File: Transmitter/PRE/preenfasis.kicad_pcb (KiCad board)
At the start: 2 copper layers, 25 x 40 mm, 24 parts, among them J1 SMA H, J2 SMA H, J3 SMA H, J4 SMA H

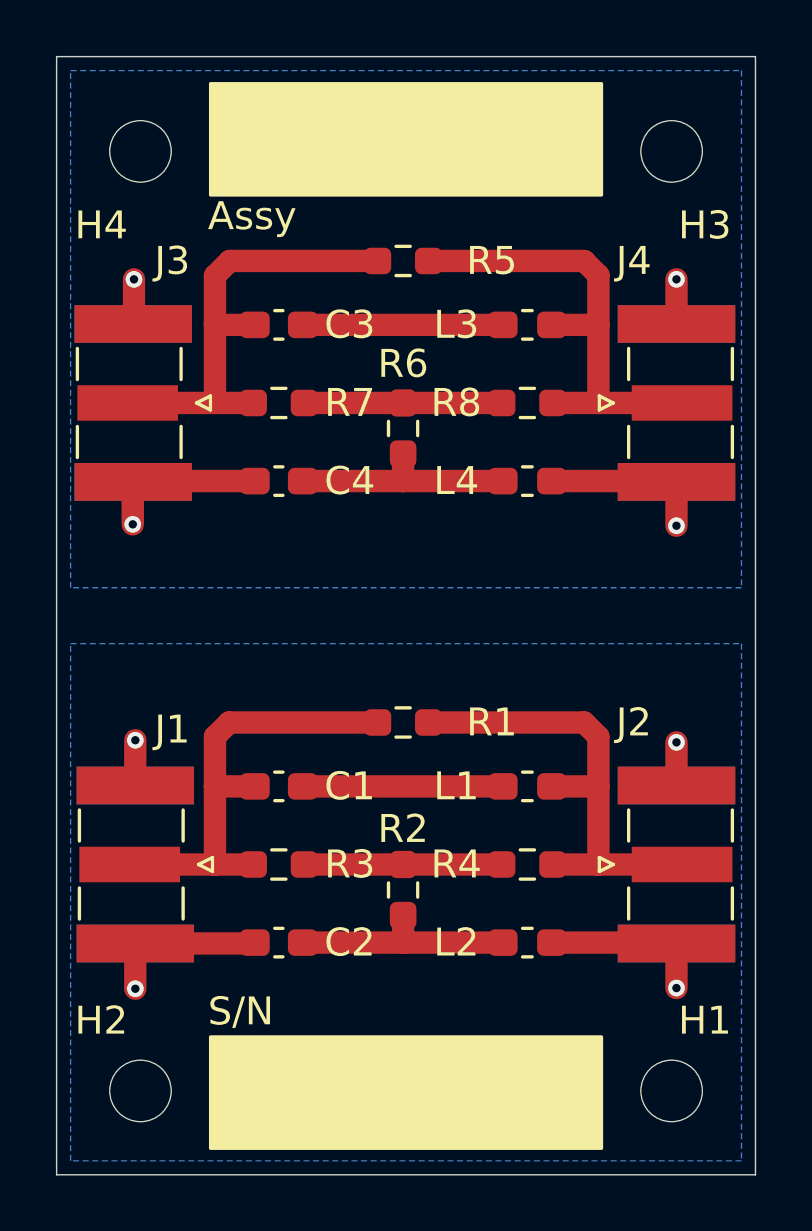
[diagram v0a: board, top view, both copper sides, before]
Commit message: v1.2 preenfasis
Se cambia el tamaño de los tornillos de M2 a M3
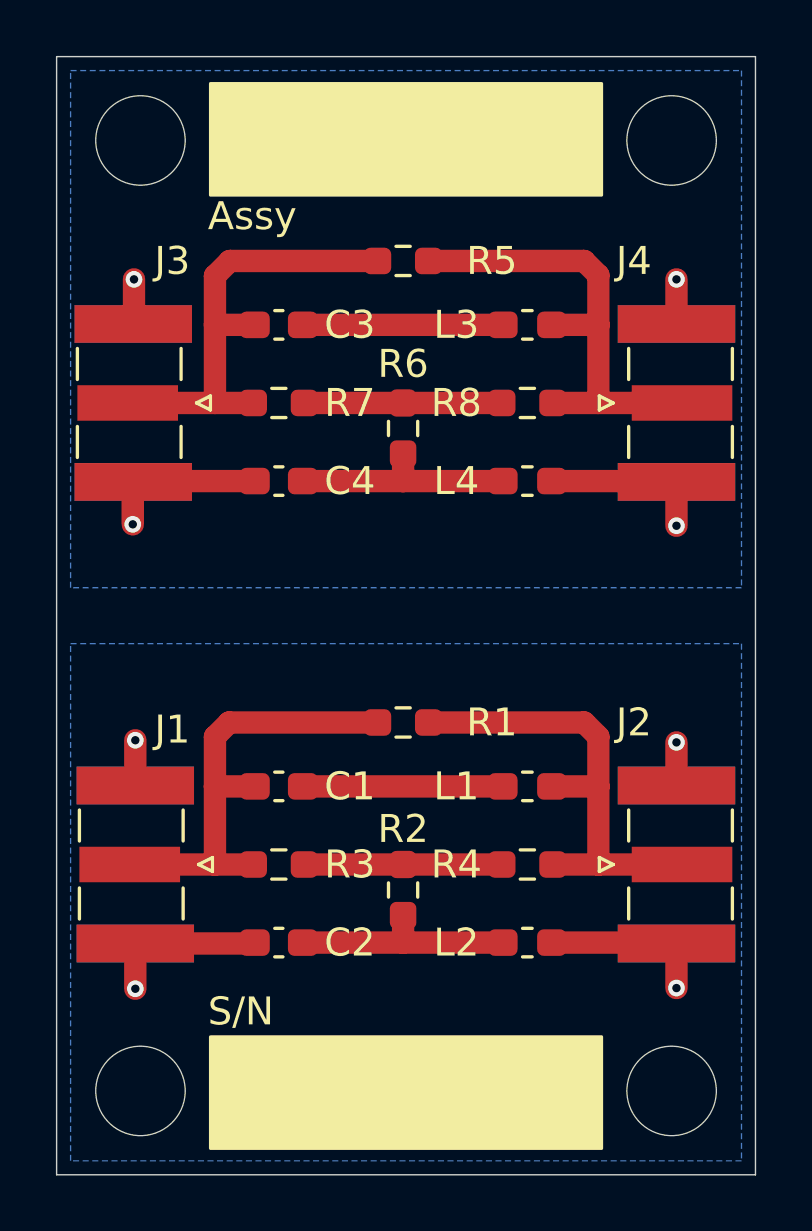
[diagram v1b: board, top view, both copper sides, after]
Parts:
- H1, H2, H3, H4: value M2 -> M3; footprint MountingHole:MountingHole_2.2mm_M2_ISO7380 -> MountingHole:MountingHole_3.2mm_M3_ISO7380
- moved H3 0.39 mm to (122.0, 63.0)
- moved H4 0.39 mm to (103.0, 63.0)
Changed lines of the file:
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@@
 	(title_block
 		(title "Filtro de preenfasis")
-		(date "2025-01-06")
-		(rev "v1.1")
+		(date "2025-01-09")
+		(rev "v1.2")
 		(company "Cotti Nicolas Gabriel")
 		(comment 1 "ncotti@frba.utn.edu.ar")
@@
 		)
 	)
-	(footprint "MountingHole:MountingHole_2.2mm_M2_ISO7380"
+	(footprint "MountingHole:MountingHole_3.2mm_M3_ISO7380"
 		(layer "F.Cu")
-		(at 122 63.3905)
-		(descr "Mounting Hole 2.2mm, no annular, M2, ISO7380")
-		(tags "mounting hole 2.2mm no annular m2 iso7380")
+		(at 122 63)
+		(descr "Mounting Hole 3.2mm, no annular, M3, ISO7380")
+		(tags "mounting hole 3.2mm no annular m3 iso7380")
 		(property "Reference" "H3"
-			(at 1.19 2.6495 0)
+			(at 0 -3.85 0)
 			(layer "F.SilkS")
+			(hide yes)
 			(effects
 				(font
@@
 			)
 		)
-		(property "Value" "M2"
-			(at 0 2.75 0)
+		(property "Value" "M3"
+			(at 0 3.85 0)
 			(layer "F.Fab")
 			(effects
@@
 			)
 		)
-		(property "Footprint" "MountingHole:MountingHole_2.2mm_M2_ISO7380"
+		(property "Footprint" "MountingHole:MountingHole_3.2mm_M3_ISO7380"
 			(at 0 0 0)
 			(layer "F.Fab")
@@
 		(fp_circle
 			(center 0 0)
-			(end 1.75 0)
+			(end 2.85 0)
 			(stroke
 				(width 0.15)
@@
 		(fp_circle
 			(center 0 0)
-			(end 2 0)
+			(end 3.1 0)
 			(stroke
 				(width 0.05)
@@
 		(pad "" np_thru_hole circle
 			(at 0 0)
-			(size 2.2 2.2)
-			(drill 2.2)
+			(size 3.2 3.2)
+			(drill 3.2)
 			(layers "*.Cu" "*.Mask")
 		)
@@
 		)
 	)
-	(footprint "MountingHole:MountingHole_2.2mm_M2_ISO7380"
+	(footprint "MountingHole:MountingHole_3.2mm_M3_ISO7380"
 		(layer "F.Cu")
-		(at 103 63.3905)
-		(descr "Mounting Hole 2.2mm, no annular, M2, ISO7380")
-		(tags "mounting hole 2.2mm no annular m2 iso7380")
+		(at 103 63)
+		(descr "Mounting Hole 3.2mm, no annular, M3, ISO7380")
+		(tags "mounting hole 3.2mm no annular m3 iso7380")
 		(property "Reference" "H4"
-			(at -1.4 2.6495 0)
+			(at 0 -3.85 0)
 			(layer "F.SilkS")
+			(hide yes)
 			(effects
 				(font
@@
 			)
 		)
-		(property "Value" "M2"
-			(at 0 2.75 0)
+		(property "Value" "M3"
+			(at 0 3.85 0)
 			(layer "F.Fab")
 			(effects
@@
 			)
 		)
-		(property "Footprint" "MountingHole:MountingHole_2.2mm_M2_ISO7380"
+		(property "Footprint" "MountingHole:MountingHole_3.2mm_M3_ISO7380"
 			(at 0 0 0)
 			(layer "F.Fab")
@@
 		(fp_circle
 			(center 0 0)
-			(end 1.75 0)
+			(end 2.85 0)
 			(stroke
 				(width 0.15)
@@
 		(fp_circle
 			(center 0 0)
-			(end 2 0)
+			(end 3.1 0)
 			(stroke
 				(width 0.05)
@@
 		(pad "" np_thru_hole circle
 			(at 0 0)
-			(size 2.2 2.2)
-			(drill 2.2)
+			(size 3.2 3.2)
+			(drill 3.2)
 			(layers "*.Cu" "*.Mask")
 		)
@@
 		)
 	)
-	(footprint "MountingHole:MountingHole_2.2mm_M2_ISO7380"
+	(footprint "MountingHole:MountingHole_3.2mm_M3_ISO7380"
 		(layer "F.Cu")
 		(at 122 97)
-		(descr "Mounting Hole 2.2mm, no annular, M2, ISO7380")
-		(tags "mounting hole 2.2mm no annular m2 iso7380")
+		(descr "Mounting Hole 3.2mm, no annular, M3, ISO7380")
+		(tags "mounting hole 3.2mm no annular m3 iso7380")
 		(property "Reference" "H1"
-			(at 1.19 -2.512 0)
+			(at 0 -3.85 0)
 			(layer "F.SilkS")
+			(hide yes)
 			(effects
 				(font
@@
 			)
 		)
-		(property "Value" "M2"
-			(at 0 2.75 0)
+		(property "Value" "M3"
+			(at 0 3.85 0)
 			(layer "F.Fab")
 			(effects
@@
 			)
 		)
-		(property "Footprint" "MountingHole:MountingHole_2.2mm_M2_ISO7380"
+		(property "Footprint" "MountingHole:MountingHole_3.2mm_M3_ISO7380"
 			(at 0 0 0)
 			(layer "F.Fab")
@@
 		(fp_circle
 			(center 0 0)
-			(end 1.75 0)
+			(end 2.85 0)
 			(stroke
 				(width 0.15)
@@
 		(fp_circle
 			(center 0 0)
-			(end 2 0)
+			(end 3.1 0)
 			(stroke
 				(width 0.05)
@@
 		(pad "" np_thru_hole circle
 			(at 0 0)
-			(size 2.2 2.2)
-			(drill 2.2)
+			(size 3.2 3.2)
+			(drill 3.2)
 			(layers "*.Cu" "*.Mask")
 		)
@@
 		)
 	)
-	(footprint "MountingHole:MountingHole_2.2mm_M2_ISO7380"
+	(footprint "MountingHole:MountingHole_3.2mm_M3_ISO7380"
 		(layer "F.Cu")
 		(at 103 97)
-		(descr "Mounting Hole 2.2mm, no annular, M2, ISO7380")
-		(tags "mounting hole 2.2mm no annular m2 iso7380")
+		(descr "Mounting Hole 3.2mm, no annular, M3, ISO7380")
+		(tags "mounting hole 3.2mm no annular m3 iso7380")
 		(property "Reference" "H2"
-			(at -1.4 -2.512 0)
+			(at 0 -3.85 0)
 			(layer "F.SilkS")
+			(hide yes)
 			(effects
 				(font
@@
 			)
 		)
-		(property "Value" "M2"
-			(at 0 2.75 0)
+		(property "Value" "M3"
+			(at 0 3.85 0)
 			(layer "F.Fab")
 			(effects
@@
 			)
 		)
-		(property "Footprint" "MountingHole:MountingHole_2.2mm_M2_ISO7380"
+		(property "Footprint" "MountingHole:MountingHole_3.2mm_M3_ISO7380"
 			(at 0 0 0)
 			(layer "F.Fab")
@@
 		(fp_circle
 			(center 0 0)
-			(end 1.75 0)
+			(end 2.85 0)
 			(stroke
 				(width 0.15)
@@
 		(fp_circle
 			(center 0 0)
-			(end 2 0)
+			(end 3.1 0)
 			(stroke
 				(width 0.05)
@@
 		(pad "" np_thru_hole circle
 			(at 0 0)
-			(size 2.2 2.2)
-			(drill 2.2)
+			(size 3.2 3.2)
+			(drill 3.2)
 			(layers "*.Cu" "*.Mask")
 		)
@@
 			(font
 				(size 1 1)
-				(thickness 0.1)
+				(thickness 0.15)
 			)
 			(justify left bottom)
@@
 			(font
 				(size 1 1)
-				(thickness 0.1)
+				(thickness 0.15)
 			)
 			(justify left bottom)
